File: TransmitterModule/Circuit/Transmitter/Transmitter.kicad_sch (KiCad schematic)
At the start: 10 parts, among them U1 ATmega328P-P, U2 NRF24L01_Breakout, U3 CH340C, U4 LM1117-3.3

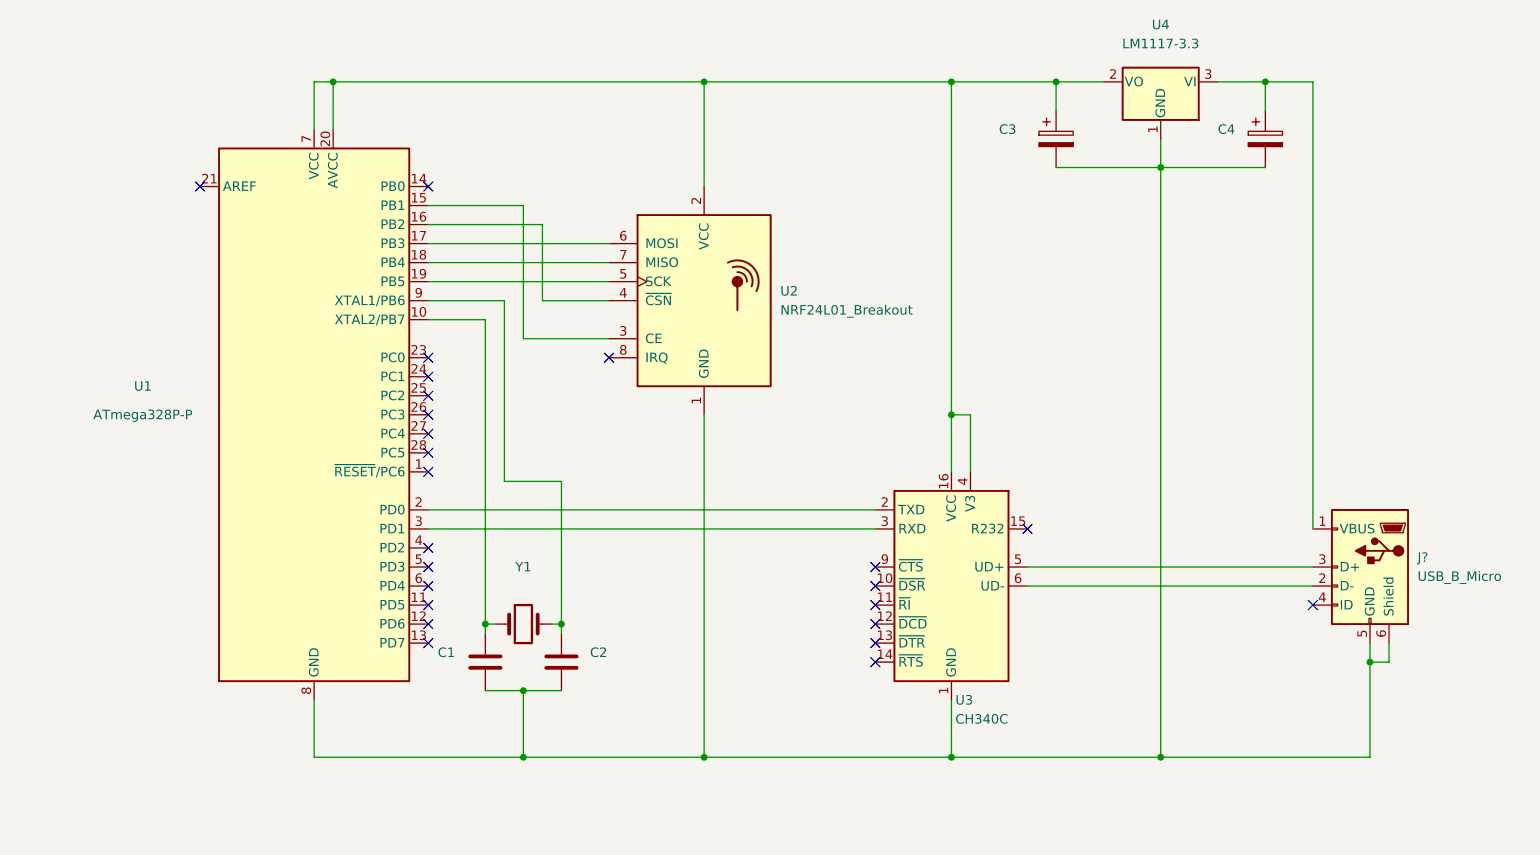
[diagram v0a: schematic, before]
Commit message: transmiter module code v1
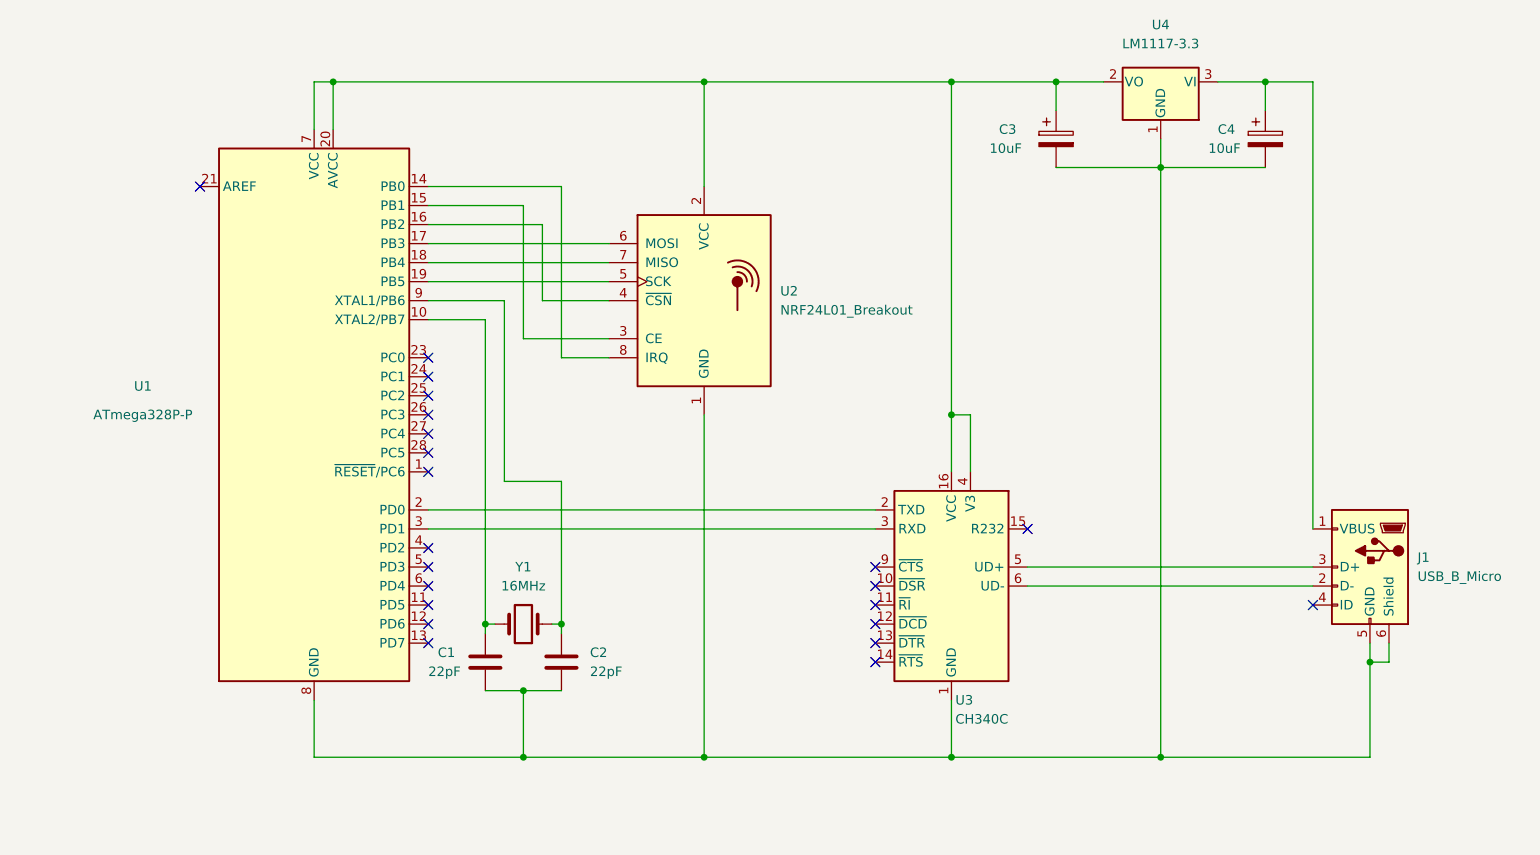
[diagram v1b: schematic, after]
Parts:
- C1, C2: value (none) -> 22pF; footprint (none) -> Capacitor_THT:C_Disc_D3.8mm_W2.6mm_P2.50mm
- C3, C4: value (none) -> 10uF
- Y1: value (none) -> 16MHz; footprint (none) -> Crystal:Crystal_HC49-U_Vertical
- gave numbers to parts that had none: 1
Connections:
- net at U1.14 (PB0): now also U2.8 (IRQ)
- no-connect marks 24 -> 22
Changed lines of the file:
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@@
   (no_connect (at 96.52 97.79))
   (no_connect (at 96.52 87.63))
-  (no_connect (at 96.52 64.77))
   (no_connect (at 96.52 118.11))
   (no_connect (at 96.52 115.57))
@@
   (no_connect (at 156.21 123.19))
   (no_connect (at 156.21 125.73))
-  (no_connect (at 120.65 87.63))
   (wire (pts (xy 120.65 85.09) (xy 109.22 85.09))
     (stroke (width 0) (type default) (color 0 0 0 0))
@@
     (stroke (width 0) (type default) (color 0 0 0 0))
   )
+  (wire (pts (xy 114.3 87.63) (xy 120.65 87.63))
+    (stroke (width 0) (type default) (color 0 0 0 0))
+  )
   (wire (pts (xy 194.31 58.42) (xy 194.31 62.23))
     (stroke (width 0) (type default) (color 0 0 0 0))
@@
     (stroke (width 0) (type default) (color 0 0 0 0))
   )
+  (wire (pts (xy 96.52 64.77) (xy 114.3 64.77))
+    (stroke (width 0) (type default) (color 0 0 0 0))
+  )
   (wire (pts (xy 83.82 50.8) (xy 133.35 50.8))
     (stroke (width 0) (type default) (color 0 0 0 0))
@@
     (stroke (width 0) (type default) (color 0 0 0 0))
   )
+  (wire (pts (xy 114.3 64.77) (xy 114.3 87.63))
+    (stroke (width 0) (type default) (color 0 0 0 0))
+  )
   (wire (pts (xy 96.52 74.93) (xy 120.65 74.93))
     (stroke (width 0) (type default) (color 0 0 0 0))
@@
   (symbol (lib_id "Connector:USB_B_Micro") (at 222.25 115.57 0) (mirror y) (unit 1)
     (in_bom yes) (on_board yes) (fields_autoplaced)
-    (property "Reference" "J?" (id 0) (at 228.6 114.2999 0)
+    (property "Reference" "J1" (id 0) (at 228.6 114.2999 0)
       (effects (font (size 1.27 1.27)) (justify right))
     )
@@
       (effects (font (size 1.27 1.27)) (justify left))
     )
-    (property "Value" "" (id 1) (at 200.66 59.69 0)
+    (property "Value" "10uF" (id 1) (at 200.66 59.69 0)
       (effects (font (size 1.27 1.27)) (justify left))
     )
@@
       (effects (font (size 1.27 1.27)) (justify left))
     )
-    (property "Value" "" (id 1) (at 118.11 129.5399 0)
-      (effects (font (size 1.27 1.27)) (justify left))
-    )
-    (property "Footprint" "" (id 2) (at 115.2652 132.08 0)
+    (property "Value" "22pF" (id 1) (at 118.11 129.5399 0)
+      (effects (font (size 1.27 1.27)) (justify left))
+    )
+    (property "Footprint" "Capacitor_THT:C_Disc_D3.8mm_W2.6mm_P2.50mm" (id 2) (at 115.2652 132.08 0)
       (effects (font (size 1.27 1.27)) hide)
     )
@@
       (effects (font (size 1.27 1.27)) (justify left))
     )
-    (property "Value" "" (id 1) (at 96.52 129.54 0)
-      (effects (font (size 1.27 1.27)) (justify left))
-    )
-    (property "Footprint" "" (id 2) (at 105.1052 132.08 0)
+    (property "Value" "22pF" (id 1) (at 96.52 129.54 0)
+      (effects (font (size 1.27 1.27)) (justify left))
+    )
+    (property "Footprint" "Capacitor_THT:C_Disc_D3.8mm_W2.6mm_P2.50mm" (id 2) (at 105.1052 132.08 0)
       (effects (font (size 1.27 1.27)) hide)
     )
@@
       (effects (font (size 1.27 1.27)) (justify left))
     )
-    (property "Value" "" (id 1) (at 171.45 59.69 0)
+    (property "Value" "10uF" (id 1) (at 171.45 59.69 0)
       (effects (font (size 1.27 1.27)) (justify left))
     )
@@
     (in_bom yes) (on_board yes) (fields_autoplaced)
     (property "Reference" "Y1" (id 0) (at 109.22 115.57 0))
-    (property "Value" "" (id 1) (at 109.22 118.11 0))
-    (property "Footprint" "" (id 2) (at 109.22 123.19 0)
+    (property "Value" "16MHz" (id 1) (at 109.22 118.11 0))
+    (property "Footprint" "Crystal:Crystal_HC49-U_Vertical" (id 2) (at 109.22 123.19 0)
       (effects (font (size 1.27 1.27)) hide)
     )
@@
     )
     (path "/1f07eb91-ef46-4237-a9f5-5823737e0d44"
-      (reference "J?") (unit 1) (value "USB_B_Micro") (footprint "Connector_USB:USB_Micro-AB_Molex_47590-0001")
+      (reference "J1") (unit 1) (value "USB_B_Micro") (footprint "Connector_USB:USB_Micro-AB_Molex_47590-0001")
     )
     (path "/a6dc1180-19c4-432b-af49-fc9179bb4519"

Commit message: transmiter audio update
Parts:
- added BZ1: Buzzer, Buzzer_Beeper:Buzzer_12x9.5RM7.6, symbol Device:Buzzer
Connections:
- net at C1.2, C2.2, C3.2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: now also BZ1.2 (+)
- net at U1.12 (PD6): now also BZ1.1 (-)
- no-connect marks 22 -> 20
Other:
- moved on the sheet: U1
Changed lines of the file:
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@@
   (junction (at 133.35 50.8) (diameter 0) (color 0 0 0 0)
   )
+  (junction (at 119.38 140.97) (diameter 0) (color 0 0 0 0)
+  )
   (junction (at 208.28 50.8) (diameter 0) (color 0 0 0 0)
   )
@@
   (junction (at 194.31 140.97) (diameter 0) (color 0 0 0 0)
   )
-  (junction (at 83.82 50.8) (diameter 0) (color 0 0 0 0)
+  (junction (at 74.93 50.8) (diameter 0) (color 0 0 0 0)
   )
   (junction (at 166.37 140.97) (diameter 0) (color 0 0 0 0)
@@
   (no_connect (at 176.53 110.49))
   (no_connect (at 156.21 120.65))
-  (no_connect (at 96.52 90.17))
-  (no_connect (at 96.52 100.33))
-  (no_connect (at 96.52 92.71))
-  (no_connect (at 96.52 95.25))
-  (no_connect (at 96.52 97.79))
-  (no_connect (at 96.52 87.63))
-  (no_connect (at 96.52 118.11))
-  (no_connect (at 96.52 115.57))
-  (no_connect (at 96.52 102.87))
-  (no_connect (at 96.52 113.03))
-  (no_connect (at 96.52 120.65))
-  (no_connect (at 96.52 123.19))
-  (no_connect (at 96.52 125.73))
+  (no_connect (at 87.63 90.17))
+  (no_connect (at 87.63 100.33))
+  (no_connect (at 87.63 92.71))
+  (no_connect (at 87.63 95.25))
+  (no_connect (at 87.63 97.79))
+  (no_connect (at 87.63 87.63))
+  (no_connect (at 87.63 118.11))
+  (no_connect (at 87.63 115.57))
+  (no_connect (at 87.63 102.87))
+  (no_connect (at 87.63 113.03))
+  (no_connect (at 87.63 120.65))
   (no_connect (at 156.21 128.27))
   (no_connect (at 156.21 115.57))
   (no_connect (at 214.63 120.65))
-  (no_connect (at 66.04 64.77))
+  (no_connect (at 57.15 64.77))
   (no_connect (at 156.21 118.11))
   (no_connect (at 156.21 123.19))
   (no_connect (at 156.21 125.73))
+  (wire (pts (xy 119.38 140.97) (xy 133.35 140.97))
+    (stroke (width 0) (type default) (color 0 0 0 0))
+  )
   (wire (pts (xy 120.65 85.09) (xy 109.22 85.09))
     (stroke (width 0) (type default) (color 0 0 0 0))
@@
     (stroke (width 0) (type default) (color 0 0 0 0))
   )
-  (wire (pts (xy 104.14 82.55) (xy 96.52 82.55))
-    (stroke (width 0) (type default) (color 0 0 0 0))
-  )
-  (wire (pts (xy 96.52 107.95) (xy 156.21 107.95))
+  (wire (pts (xy 104.14 82.55) (xy 87.63 82.55))
+    (stroke (width 0) (type default) (color 0 0 0 0))
+  )
+  (wire (pts (xy 87.63 107.95) (xy 156.21 107.95))
     (stroke (width 0) (type default) (color 0 0 0 0))
   )
@@
     (stroke (width 0) (type default) (color 0 0 0 0))
   )
-  (wire (pts (xy 109.22 140.97) (xy 133.35 140.97))
+  (wire (pts (xy 109.22 140.97) (xy 119.38 140.97))
     (stroke (width 0) (type default) (color 0 0 0 0))
   )
@@
     (stroke (width 0) (type default) (color 0 0 0 0))
   )
-  (wire (pts (xy 81.28 50.8) (xy 83.82 50.8))
+  (wire (pts (xy 72.39 50.8) (xy 74.93 50.8))
     (stroke (width 0) (type default) (color 0 0 0 0))
   )
@@
     (stroke (width 0) (type default) (color 0 0 0 0))
   )
+  (wire (pts (xy 87.63 123.19) (xy 91.44 123.19))
+    (stroke (width 0) (type default) (color 0 0 0 0))
+  )
   (wire (pts (xy 106.68 104.14) (xy 114.3 104.14))
     (stroke (width 0) (type default) (color 0 0 0 0))
@@
     (stroke (width 0) (type default) (color 0 0 0 0))
   )
+  (wire (pts (xy 107.95 146.05) (xy 119.38 146.05))
+    (stroke (width 0) (type default) (color 0 0 0 0))
+  )
   (wire (pts (xy 194.31 140.97) (xy 166.37 140.97))
     (stroke (width 0) (type default) (color 0 0 0 0))
@@
     (stroke (width 0) (type default) (color 0 0 0 0))
   )
-  (wire (pts (xy 81.28 57.15) (xy 81.28 50.8))
+  (wire (pts (xy 72.39 57.15) (xy 72.39 50.8))
     (stroke (width 0) (type default) (color 0 0 0 0))
   )
@@
     (stroke (width 0) (type default) (color 0 0 0 0))
   )
-  (wire (pts (xy 81.28 140.97) (xy 109.22 140.97))
+  (wire (pts (xy 72.39 140.97) (xy 109.22 140.97))
     (stroke (width 0) (type default) (color 0 0 0 0))
   )
@@
     (stroke (width 0) (type default) (color 0 0 0 0))
   )
-  (wire (pts (xy 96.52 69.85) (xy 111.76 69.85))
+  (wire (pts (xy 87.63 69.85) (xy 111.76 69.85))
     (stroke (width 0) (type default) (color 0 0 0 0))
   )
@@
     (stroke (width 0) (type default) (color 0 0 0 0))
   )
-  (wire (pts (xy 96.52 64.77) (xy 114.3 64.77))
-    (stroke (width 0) (type default) (color 0 0 0 0))
-  )
-  (wire (pts (xy 83.82 50.8) (xy 133.35 50.8))
+  (wire (pts (xy 87.63 64.77) (xy 114.3 64.77))
+    (stroke (width 0) (type default) (color 0 0 0 0))
+  )
+  (wire (pts (xy 74.93 50.8) (xy 133.35 50.8))
     (stroke (width 0) (type default) (color 0 0 0 0))
   )
@@
     (stroke (width 0) (type default) (color 0 0 0 0))
   )
+  (wire (pts (xy 91.44 123.19) (xy 91.44 146.05))
+    (stroke (width 0) (type default) (color 0 0 0 0))
+  )
   (wire (pts (xy 109.22 85.09) (xy 109.22 67.31))
     (stroke (width 0) (type default) (color 0 0 0 0))
   )
-  (wire (pts (xy 96.52 72.39) (xy 120.65 72.39))
+  (wire (pts (xy 87.63 72.39) (xy 120.65 72.39))
     (stroke (width 0) (type default) (color 0 0 0 0))
   )
@@
     (stroke (width 0) (type default) (color 0 0 0 0))
   )
+  (wire (pts (xy 119.38 140.97) (xy 119.38 146.05))
+    (stroke (width 0) (type default) (color 0 0 0 0))
+  )
   (wire (pts (xy 166.37 140.97) (xy 166.37 133.35))
     (stroke (width 0) (type default) (color 0 0 0 0))
   )
-  (wire (pts (xy 83.82 50.8) (xy 83.82 57.15))
+  (wire (pts (xy 74.93 50.8) (xy 74.93 57.15))
     (stroke (width 0) (type default) (color 0 0 0 0))
   )
@@
     (stroke (width 0) (type default) (color 0 0 0 0))
   )
-  (wire (pts (xy 96.52 77.47) (xy 120.65 77.47))
+  (wire (pts (xy 87.63 77.47) (xy 120.65 77.47))
     (stroke (width 0) (type default) (color 0 0 0 0))
   )
@@
     (stroke (width 0) (type default) (color 0 0 0 0))
   )
-  (wire (pts (xy 96.52 74.93) (xy 120.65 74.93))
-    (stroke (width 0) (type default) (color 0 0 0 0))
-  )
-  (wire (pts (xy 81.28 133.35) (xy 81.28 140.97))
+  (wire (pts (xy 87.63 74.93) (xy 120.65 74.93))
+    (stroke (width 0) (type default) (color 0 0 0 0))
+  )
+  (wire (pts (xy 72.39 133.35) (xy 72.39 140.97))
     (stroke (width 0) (type default) (color 0 0 0 0))
   )
@@
     (stroke (width 0) (type default) (color 0 0 0 0))
   )
-  (wire (pts (xy 96.52 80.01) (xy 106.68 80.01))
+  (wire (pts (xy 87.63 80.01) (xy 106.68 80.01))
     (stroke (width 0) (type default) (color 0 0 0 0))
   )
@@
     (stroke (width 0) (type default) (color 0 0 0 0))
   )
-  (wire (pts (xy 96.52 110.49) (xy 156.21 110.49))
+  (wire (pts (xy 87.63 110.49) (xy 156.21 110.49))
     (stroke (width 0) (type default) (color 0 0 0 0))
   )
@@
     (stroke (width 0) (type default) (color 0 0 0 0))
   )
-  (wire (pts (xy 109.22 67.31) (xy 96.52 67.31))
+  (wire (pts (xy 109.22 67.31) (xy 87.63 67.31))
     (stroke (width 0) (type default) (color 0 0 0 0))
   )
@@
   )
   (wire (pts (xy 105.41 123.19) (xy 104.14 123.19))
+    (stroke (width 0) (type default) (color 0 0 0 0))
+  )
+  (wire (pts (xy 91.44 146.05) (xy 102.87 146.05))
     (stroke (width 0) (type default) (color 0 0 0 0))
   )
@@
     (pin "6")
   )
+  (symbol (lib_id "Device:Buzzer") (at 105.41 148.59 90) (mirror x) (unit 1)
+    (in_bom yes) (on_board yes) (fields_autoplaced)
+    (property "Reference" "BZ1" (id 0) (at 109.22 148.0819 90)
+      (effects (font (size 1.27 1.27)) (justify right))
+    )
+    (property "Value" "Buzzer" (id 1) (at 109.22 150.6219 90)
+      (effects (font (size 1.27 1.27)) (justify right))
+    )
+    (property "Footprint" "Buzzer_Beeper:Buzzer_12x9.5RM7.6" (id 2) (at 102.87 147.955 90)
+      (effects (font (size 1.27 1.27)) hide)
+    )
+    (property "Datasheet" "~" (id 3) (at 102.87 147.955 90)
+      (effects (font (size 1.27 1.27)) hide)
+    )
+    (pin "1")
+    (pin "2")
+  )
   (symbol (lib_id "Device:C_Polarized") (at 208.28 58.42 0) (unit 1)
     (in_bom yes) (on_board yes)
@@
     (pin "2")
   )
-  (symbol (lib_id "MCU_Microchip_ATmega:ATmega328P-P") (at 81.28 95.25 0) (unit 1)
+  (symbol (lib_id "MCU_Microchip_ATmega:ATmega328P-P") (at 72.39 95.25 0) (unit 1)
     (in_bom yes) (on_board yes)
-    (property "Reference" "U1" (id 0) (at 58.42 91.44 0))
-    (property "Value" "ATmega328P-P" (id 1) (at 58.42 95.25 0))
-    (property "Footprint" "Package_DIP:DIP-28_W7.62mm" (id 2) (at 81.28 95.25 0)
+    (property "Reference" "U1" (id 0) (at 49.53 91.44 0))
+    (property "Value" "ATmega328P-P" (id 1) (at 49.53 95.25 0))
+    (property "Footprint" "Package_DIP:DIP-28_W7.62mm" (id 2) (at 72.39 95.25 0)
       (effects (font (size 1.27 1.27) italic) hide)
     )
-    (property "Datasheet" "http://ww1.microchip.com/downloads/en/DeviceDoc/ATmega328_P%20AVR%20MCU%20with%20picoPower%20Technology%20Data%20Sheet%2040001984A.pdf" (id 3) (at 81.28 95.25 0)
+    (property "Datasheet" "http://ww1.microchip.com/downloads/en/DeviceDoc/ATmega328_P%20AVR%20MCU%20with%20picoPower%20Technology%20Data%20Sheet%2040001984A.pdf" (id 3) (at 72.39 95.25 0)
       (effects (font (size 1.27 1.27)) hide)
     )
@@
   )
   (symbol_instances
+    (path "/2089a151-13d4-455b-b3a5-9741b7d7a885"
+      (reference "BZ1") (unit 1) (value "Buzzer") (footprint "Buzzer_Beeper:Buzzer_12x9.5RM7.6")
+    )
     (path "/45e3a90b-d22e-4e72-a1c6-03596189a34c"
       (reference "C1") (unit 1) (value "22pF") (footprint "Capacitor_THT:C_Disc_D3.8mm_W2.6mm_P2.50mm")

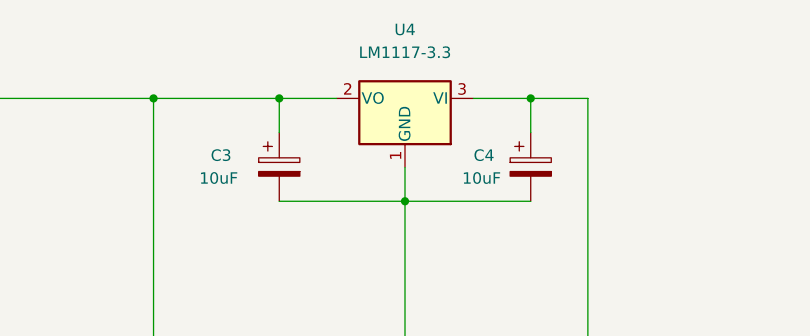
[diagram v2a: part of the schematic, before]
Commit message: stabilizator update in circuits
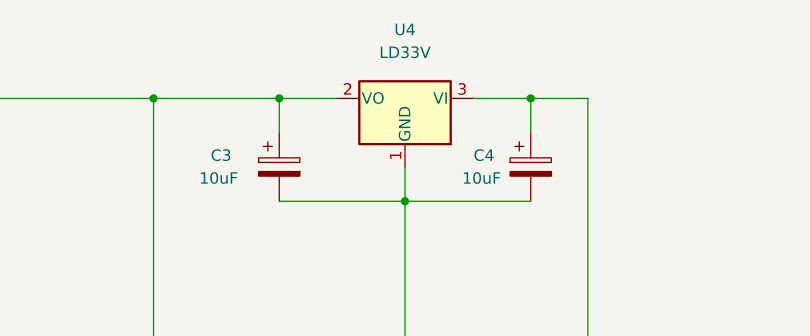
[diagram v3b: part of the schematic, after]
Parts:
- U4: value LM1117-3.3 -> LD33V
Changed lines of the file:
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@@
     (in_bom yes) (on_board yes) (fields_autoplaced)
     (property "Reference" "U4" (id 0) (at 194.31 43.18 0))
-    (property "Value" "LM1117-3.3" (id 1) (at 194.31 45.72 0))
+    (property "Value" "LD33V" (id 1) (at 194.31 45.72 0))
     (property "Footprint" "Package_TO_SOT_SMD:TO-252-2" (id 2) (at 194.31 50.8 0)
       (effects (font (size 1.27 1.27)) hide)
@@
     )
     (path "/33877aa3-5be8-4906-b28a-c47c8e080931"
-      (reference "U4") (unit 1) (value "LM1117-3.3") (footprint "Package_TO_SOT_SMD:TO-252-2")
+      (reference "U4") (unit 1) (value "LD33V") (footprint "Package_TO_SOT_SMD:TO-252-2")
     )
     (path "/9b2c3896-c54b-4cf2-8fa5-0036fca2d447"
